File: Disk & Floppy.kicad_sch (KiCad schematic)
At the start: 37 parts, among them J11 External FDD, J12 External HDD, J13 FDD Power, J7 Internal FDD, U18 74HC74, U19 74HC244, U20 74HC245, U22 74HS05, U37 DMA, U38 WD1772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

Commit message: motherboard: Fixed a missing connection in the HDD interface drive circuitry
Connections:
- net +5V: now also U4.10 (~{S}), U4.13 (~{R})
- net GND: now also U4.11 (C), U4.12 (D)
- net at U4.1 (~{R}), U4.2 (D): now also U37.22 (~{FDCS}), U38.1 (~{CS})
- no-connect marks 8 -> 10
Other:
- moved on the sheet: U4B

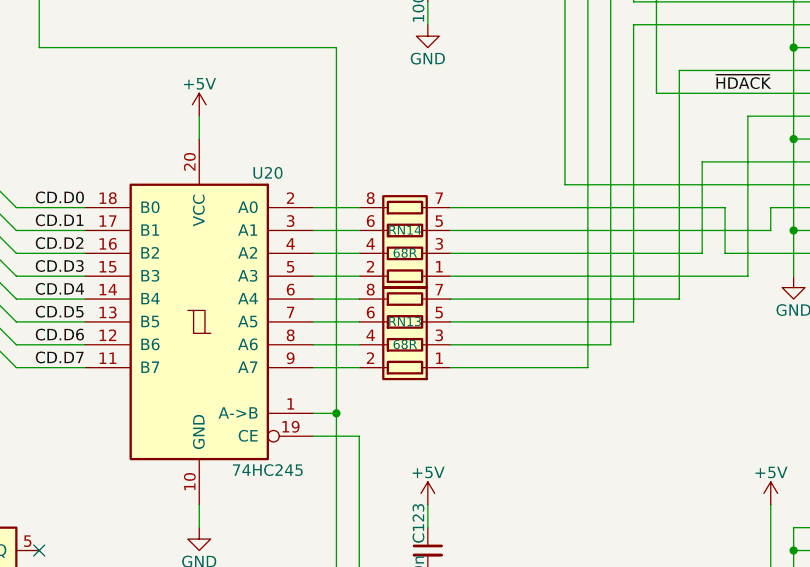
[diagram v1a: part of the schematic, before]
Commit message: motherboard: Routed in the last of the HDD control buffers, and begun routing in BLiTTER
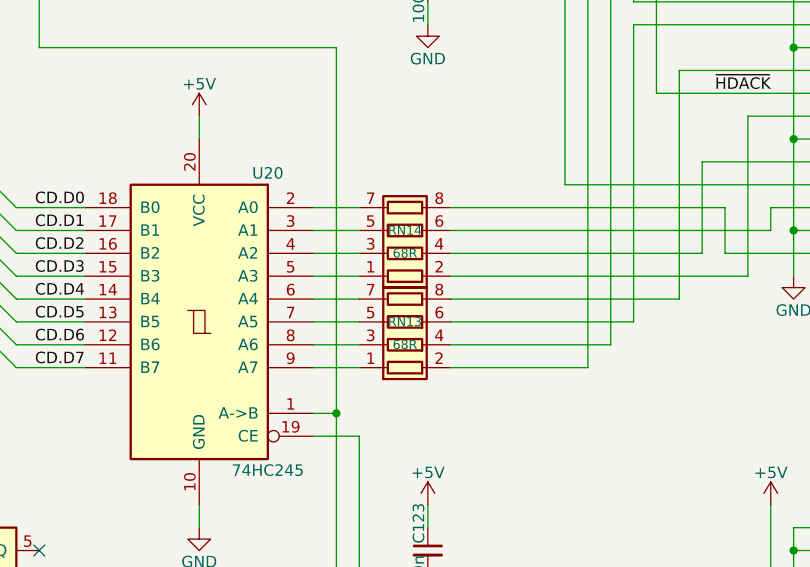
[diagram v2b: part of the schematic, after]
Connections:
- net at U20.2 (A0): now also RN14.7 (R2.2); no longer RN14.8 (R1.2)
- net at U20.3 (A1): now also RN14.5 (R4.2); no longer RN14.6 (R3.2)
- net at U20.4 (A2): now also RN14.3 (R3.1); no longer RN14.4 (R4.1)
- net at U20.5 (A3): now also RN14.1 (R1.1); no longer RN14.2 (R2.1)
- net at U20.6 (A4): now also RN13.7 (R2.2); no longer RN13.8 (R1.2)
- net at U20.7 (A5): now also RN13.5 (R4.2); no longer RN13.6 (R3.2)
- net at U20.8 (A6): now also RN13.3 (R3.1); no longer RN13.4 (R4.1)
- net at U20.9 (A7): now also RN13.1 (R1.1); no longer RN13.2 (R2.1)
- net at J12.8: now also RN13.2 (R2.1); no longer RN13.1 (R1.1)
- net at J12.7: now also RN13.4 (R4.1); no longer RN13.3 (R3.1)
- net at J12.6: now also RN13.6 (R3.2); no longer RN13.5 (R4.2)
- net at J12.5: now also RN13.8 (R1.2); no longer RN13.7 (R2.2)
- net at J12.1: now also RN14.8 (R1.2); no longer RN14.7 (R2.2)
- net at J12.2: now also RN14.6 (R3.2); no longer RN14.5 (R4.2)
- net at J12.3: now also RN14.4 (R4.1); no longer RN14.3 (R3.1)
- net at J12.4: now also RN14.2 (R2.1); no longer RN14.1 (R1.1)
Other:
- moved on the sheet: RN13, RN14
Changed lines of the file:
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@@
 	(symbol
 		(lib_id "dragonmux:R_Pack04_OddEven")
-		(at 111.76 127 90)
+		(at 111.76 127 270)
+		(mirror x)
 		(unit 1)
 		(exclude_from_sim no)
@@
 		)
 		(property "Description" "4 resistor network, parallel topology"
-			(at 124.46 128.27 0)
+			(at 99.06 128.27 0)
 			(effects
 				(font
@@
 	(symbol
 		(lib_id "dragonmux:R_Pack04_OddEven")
-		(at 111.76 116.84 90)
+		(at 111.76 116.84 270)
+		(mirror x)
 		(unit 1)
 		(exclude_from_sim no)
@@
 		)
 		(property "Description" "4 resistor network, parallel topology"
-			(at 124.46 118.11 0)
-			(effects
-				(font
+			(at 99.06 118.11 0)
+			(effects
+				(font
